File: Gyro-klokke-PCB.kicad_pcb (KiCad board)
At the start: 2 copper layers, 40.6 x 25.4 mm, 21 parts, among them J1 Conn_01x04_Male, J2 Conn_01x04_Male, J3 Conn_01x03_Male, J4 Conn_02x05_Odd_Even, SW1 SW_Push, SW2 SW_Push, U1 STM32F030F4Px, U2 LB1948MC, U3 LB1948MC, Y1 Crystal_Small

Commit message: Kretskort ferdig v1.0
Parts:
- added C5: 100nF, Capacitor_SMD:C_0805_2012Metric, F.Cu at (174.5, 120.1)
- added J5: Conn_01x01_Female, MountingHole:MountingHole_2.2mm_M2_ISO14580_Pad, F.Cu at (184.9, 107.7)
- added J6: Conn_01x01_Female, MountingHole:MountingHole_2.2mm_M2_ISO14580_Pad, F.Cu at (161.0, 126.7)
- J3: footprint Connector_Molex:Molex_PicoBlade_53398-0371_1x03-1MP_P1.25mm_Vertical -> Connector_Molex:Molex_PicoBlade_53398-0471_1x04-1MP_P1.25mm_Vertical
- moved SW1 22.6 mm to (160.3, 107.2)
- moved R1 20.9 mm to (181.9, 118.9)
- moved R2 15.9 mm to (168.4, 119.9), turned to 90 degrees
- moved C3 12.7 mm to (167.1, 110.7), turned to 180 degrees
- moved C1 11.9 mm to (164.6, 112.3)
- moved C4 8.69 mm to (167.1, 117.3), turned to 180 degrees
- moved R5 8.15 mm to (159.8, 109.7), turned to 180 degrees
- moved R3 6.19 mm to (162.6, 112.0), turned to 90 degrees
- moved R6 5.98 mm to (164.1, 109.7), turned to 180 degrees
- moved SW2 5.91 mm to (165.9, 107.2)
- moved Y1 4.13 mm to (168.1, 114.0)
- moved R4 3.34 mm to (160.5, 112.0), turned to 90 degrees
- moved J3 2.05 mm to (174.8, 109.0)
- moved J4 1.20 mm to (174.2, 125.0)
- moved C2 0.77 mm to (158.5, 112.3), turned to 90 degrees
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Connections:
- J3 pad 2: uart-TX -> uart-RX
- J3 pad 3: +3V3 -> uart-TX
- SW1 pad 1: GNDREF -> Net-(R4-Pad2)
- SW1 pad 2: Net-(R4-Pad2) -> GNDREF
- U1 pad 18: (no net) -> uart-RX
- U2 pad 1: VCC -> +3V3
- U3 pad 1: VCC -> +3V3
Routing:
- net +3V3: track 0.00 -> 74.9 mm, vias 0 -> 2
- net GNDREF: track 0.00 -> 71.7 mm, vias 0 -> 4
- net Net-(C2-Pad1): track 0.00 -> 30.5 mm, vias 0 -> 2
- net mot1-B1: track 0.00 -> 18.4 mm, vias 0 -> 2
- net mot1-B2: track 0.00 -> 17.6 mm, vias 0 -> 2
- net Net-(C1-Pad1): track 0.00 -> 17.4 mm, vias 0 -> 2
- net SWD-SWIO: track 0.00 -> 15.8 mm, vias 0 -> 2
- net SWD-SWCLK: track 0.00 -> 15.4 mm, vias 0 -> 3
- net Net-(R1-Pad1): track 0.00 -> 13.6 mm, vias 0 -> 2
- net mot1-A2: track 0.00 -> 13.5 mm, vias 0 -> 2
- net mot1-A1: track 0.00 -> 13.1 mm, vias 0 -> 2
- net mot2-A1: track 0.00 -> 10.9 mm
- net mot2-A2: track 0.00 -> 8.86 mm
- net Net-(R4-Pad2): track 0.00 -> 7.81 mm
- net Net-(R3-Pad2): track 0.00 -> 7.50 mm
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- added copper zone on B.Cu, net GNDREF
- added copper zone on F.Cu, net GNDREF
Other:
- board size 40.6 x 25.4 mm -> 37.3 x 24.1 mm

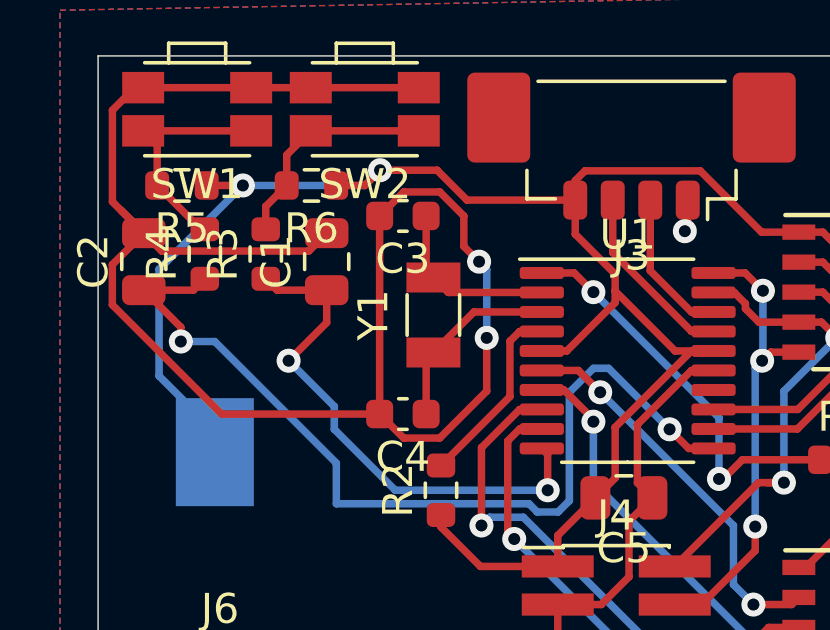
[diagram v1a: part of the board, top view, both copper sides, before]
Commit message: Kretskort ferdig v1.0, la til gnd på rtc cap
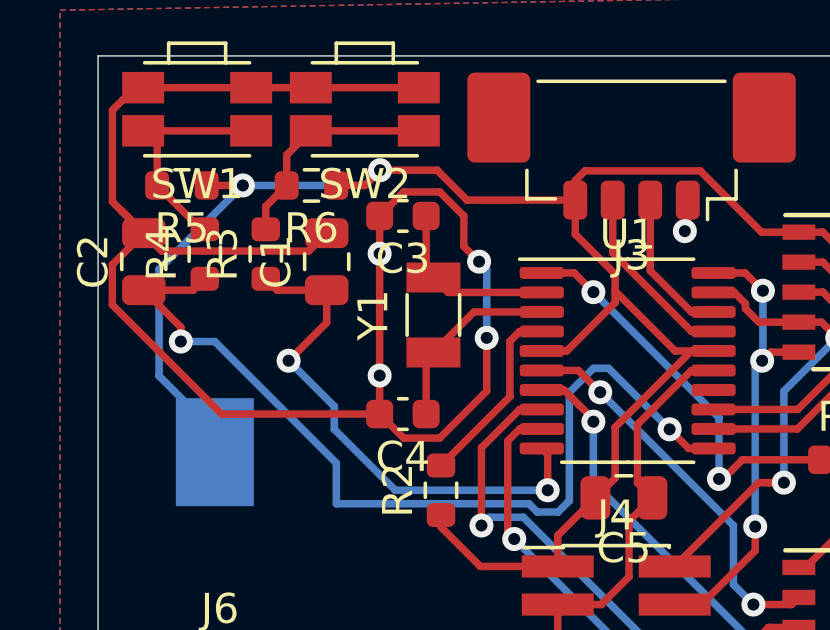
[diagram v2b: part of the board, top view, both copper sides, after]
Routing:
- net GNDREF: vias 4 -> 6

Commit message: rev1.0 RC1
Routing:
- net nRESET: track 6.29 -> 20.1 mm, vias 0 -> 2
- net GNDREF: track 71.7 -> 75.8 mm

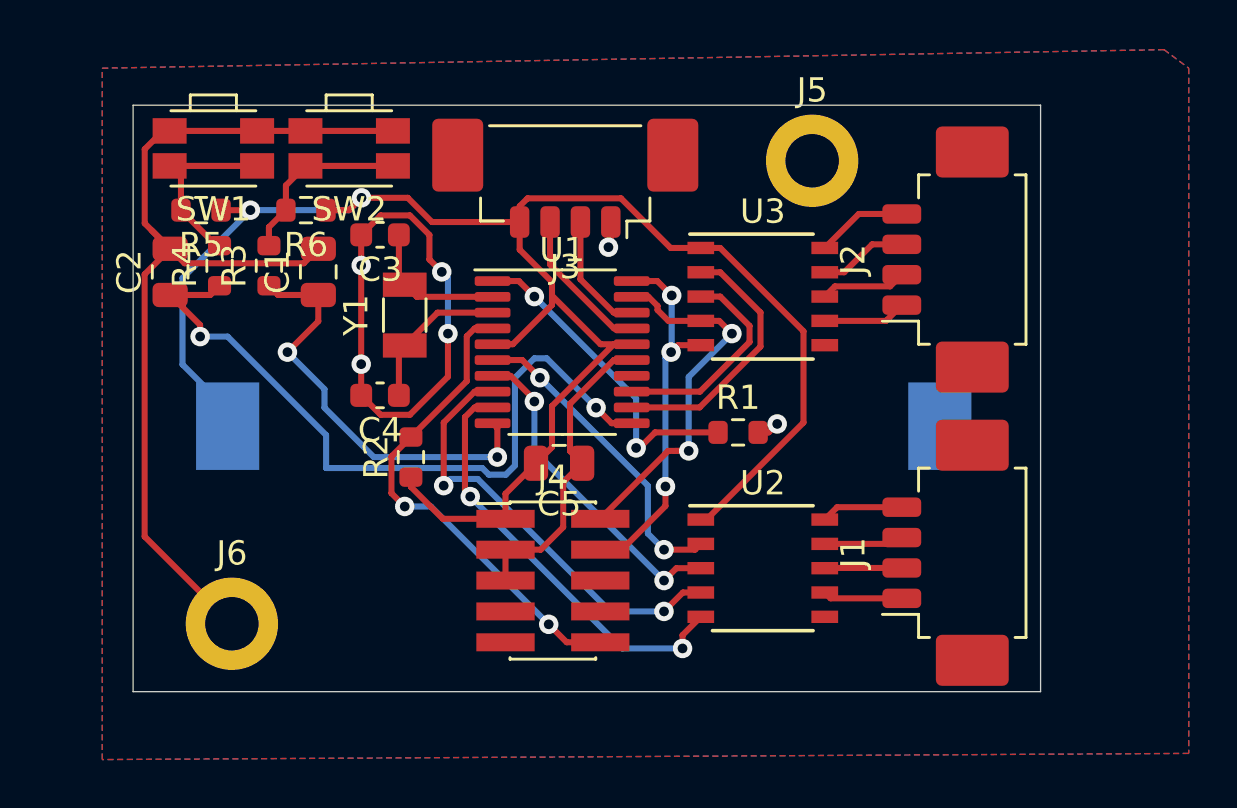
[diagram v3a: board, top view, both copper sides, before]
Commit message: endret stm32 til nrf
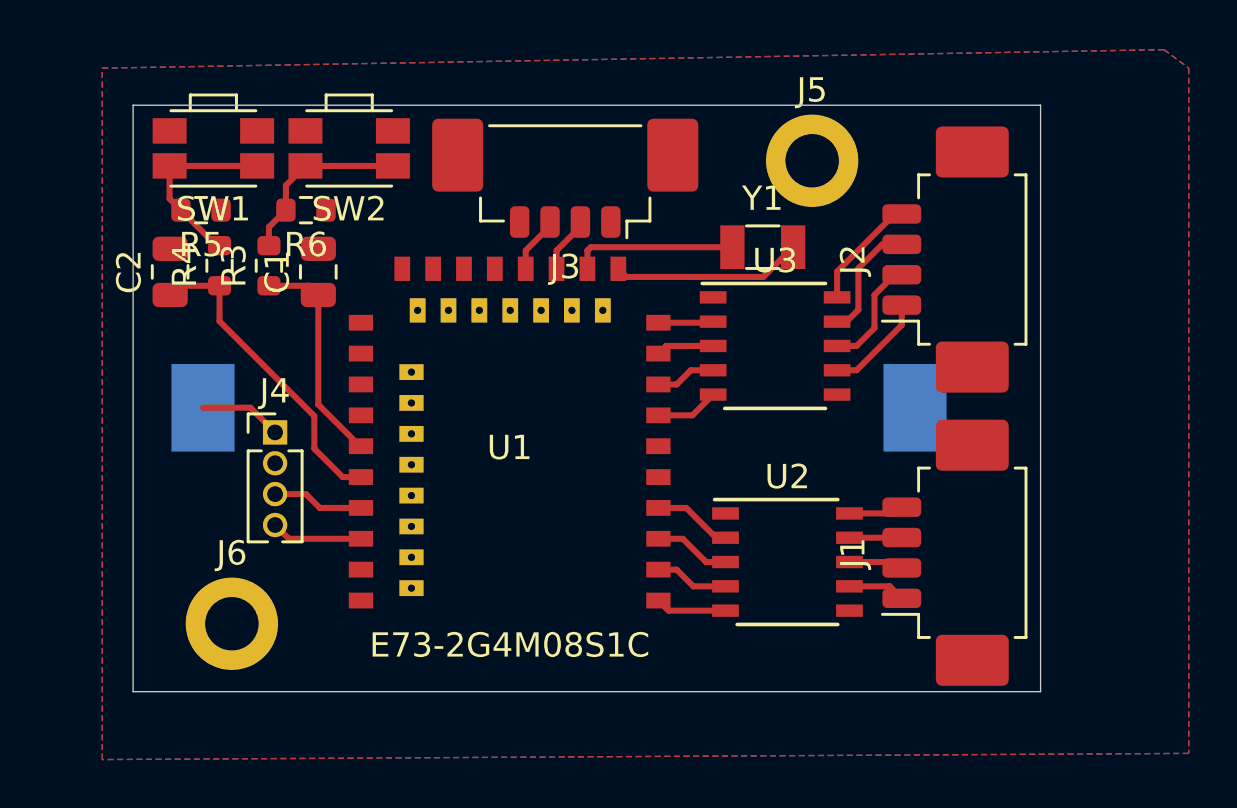
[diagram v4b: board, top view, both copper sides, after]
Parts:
- removed C3, C4: C_Small, Capacitor_SMD:C_0603_1608Metric
- removed C5: 100nF, Capacitor_SMD:C_0805_2012Metric
- removed R1: R_Small, Resistor_SMD:R_0603_1608Metric
- removed R2: 10K, Resistor_SMD:R_0603_1608Metric
- J4: value Conn_02x05_Odd_Even -> Conn_01x04_Male; footprint Connector_PinHeader_1.27mm:PinHeader_2x05_P1.27mm_Vertical_SMD -> Connector_PinHeader_1.27mm:PinHeader_1x04_P1.27mm_Vertical
- U1: value STM32F030F4Px -> E73-2G4M08S1C-52840; footprint Package_SO:TSSOP-20_4.4x6.5mm_P0.65mm -> nrfmicro:E73-2G4M08S1C-52840
- moved Y1 15.0 mm to (182.9, 111.3), turned to 0 degrees
- moved J4 13.0 mm to (162.8, 118.9)
- moved U1 4.38 mm to (172.5, 111.8), turned to 270 degrees
- moved U3 2.09 mm to (183.4, 115.3)
- moved BT1 1.27 mm to (174.5, 117.9)
- moved U2 1.05 mm to (183.9, 124.2)
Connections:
- C1 pad 1: Net-(C1-Pad1) -> sw2
- C2 pad 1: Net-(C2-Pad1) -> sw1
- J4 pad 2: SWD-SWIO -> GNDREF
- J4 pad 3: GNDREF -> SWD
- J4 pad 4: SWD-SWCLK -> SWC
- R3 pad 1: Net-(C1-Pad1) -> sw2
- R4 pad 1: Net-(C2-Pad1) -> sw1
- U1 pad 1: Net-(R1-Pad1) -> mot1-B2
- U1 pad 10: Net-(C1-Pad1) -> mot2-A1
- U1 pad 11: Net-(C2-Pad1) -> Net-(U1-Pad11)
- U1 pad 12: mot2-A1 -> (no net)
- U1 pad 13: mot2-A2 -> Net-(U1-Pad13)
- U1 pad 15: GNDREF -> uart-RX
- U1 pad 16: +3V3 -> (no net)
- U1 pad 18: uart-RX -> (no net)
- U1 pad 19: SWD-SWIO -> +3V3
- U1 pad 2: Net-(C3-Pad1) -> mot1-B1
- U1 pad 20: SWD-SWCLK -> (no net)
- U1 pad 3: Net-(C4-Pad1) -> mot1-A2
- U1 pad 4: nRESET -> mot1-A1
- U1 pad 5: +3V3 -> GNDREF
- U1 pad 6: mot1-A1 -> (no net)
- U1 pad 7: mot1-A2 -> mot2-B2
- U1 pad 8: mot1-B1 -> mot2-B1
- U1 pad 9: mot1-B2 -> mot2-A2
- U3 pad 4: SWD-SWIO -> mot2-B1
- U3 pad 5: SWD-SWCLK -> mot2-B2
- Y1 pad 1: Net-(C3-Pad1) -> Net-(U1-Pad11)
- Y1 pad 2: Net-(C4-Pad1) -> Net-(U1-Pad13)
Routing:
- net GNDREF: track 75.8 -> 0.00 mm, vias 6 -> 0
- net +3V3: track 74.9 -> 3.39 mm, vias 2 -> 0
- net Net-(C2-Pad1): track 30.5 -> 0.00 mm, vias 2 -> 0
- net nRESET: track 20.1 -> 0.00 mm, vias 2 -> 0
- net Net-(C1-Pad1): track 17.4 -> 0.00 mm, vias 2 -> 0
- net SWD-SWIO: track 15.8 -> 0.00 mm, vias 2 -> 0
- net SWD-SWCLK: track 15.4 -> 0.00 mm, vias 3 -> 0
- net mot1-B1: track 18.4 -> 3.05 mm, vias 2 -> 0
- net mot1-B2: track 17.6 -> 2.93 mm, vias 2 -> 0
- net Net-(R1-Pad1): track 13.6 -> 0.00 mm, vias 2 -> 0
- net sw1: track 0.00 -> 12.9 mm
- net mot1-A2: track 13.5 -> 3.16 mm, vias 2 -> 0
- net mot1-A1: track 13.1 -> 3.27 mm, vias 2 -> 0
- net sw2: track 0.00 -> 9.16 mm
- net mot2-A1: track 10.9 -> 2.27 mm
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
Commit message: Fikset ting
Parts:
- removed J3: Conn_01x03_Male, Connector_Molex:Molex_PicoBlade_53398-0471_1x04-1MP_P1.25mm_Vertical
- added J7: USB_C_Receptacle_USB2.0, nrfmicro:USB-C_C168688, F.Cu at (174.8, 102.1)
- added J8: Conn_01x02_Female, Connector_PinHeader_1.27mm:PinHeader_2x01_P1.27mm_Vertical, F.Cu at (182.0, 106.9)
- added R1: 5.7K, Resistor_SMD:R_0603_1608Metric, F.Cu at (179.2, 110.6)
- added R2: 5.7K, Resistor_SMD:R_0603_1608Metric, F.Cu at (169.4, 110.5)
- moved J5 0.23 mm to (185.1, 107.7)
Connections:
- U1 pad 15: uart-RX -> (no net)
- U1 pad 17: uart-TX -> (no net)
- U1 pad 27: (no net) -> Net-(J8-Pad2)
- U1 pad 29: (no net) -> /D-
- U1 pad 31: (no net) -> /D+
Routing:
- net GNDREF: track 0.00 -> 58.6 mm, vias 0 -> 1
- net +3V3: track 3.39 -> 61.8 mm, vias 0 -> 7
- net Net-(J8-Pad2): track 0.00 -> 19.9 mm, vias 0 -> 1
- net /D+: track 0.00 -> 18.6 mm, vias 0 -> 1
- net /D-: track 0.00 -> 17.5 mm, vias 0 -> 3
- net /VBUS: track 0.00 -> 11.6 mm
- net Net-(J7-PadB5): track 0.00 -> 3.77 mm
- net Net-(J7-PadA5): track 0.00 -> 3.34 mm
- net uart-TX: track 2.34 -> 0.00 mm
- net uart-RX: track 2.33 -> 0.00 mm
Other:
- outline, holes or cut-outs redrawn
- net class Default removed
